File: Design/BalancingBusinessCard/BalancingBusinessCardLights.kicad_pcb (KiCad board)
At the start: 2 copper layers, 51 x 89 mm, 38 parts, among them J101 Conn_02x01, SW101 SW_Push, U101 ATtiny261A-MU, U401 LIS3DHTR, U402 MCP1640DCH

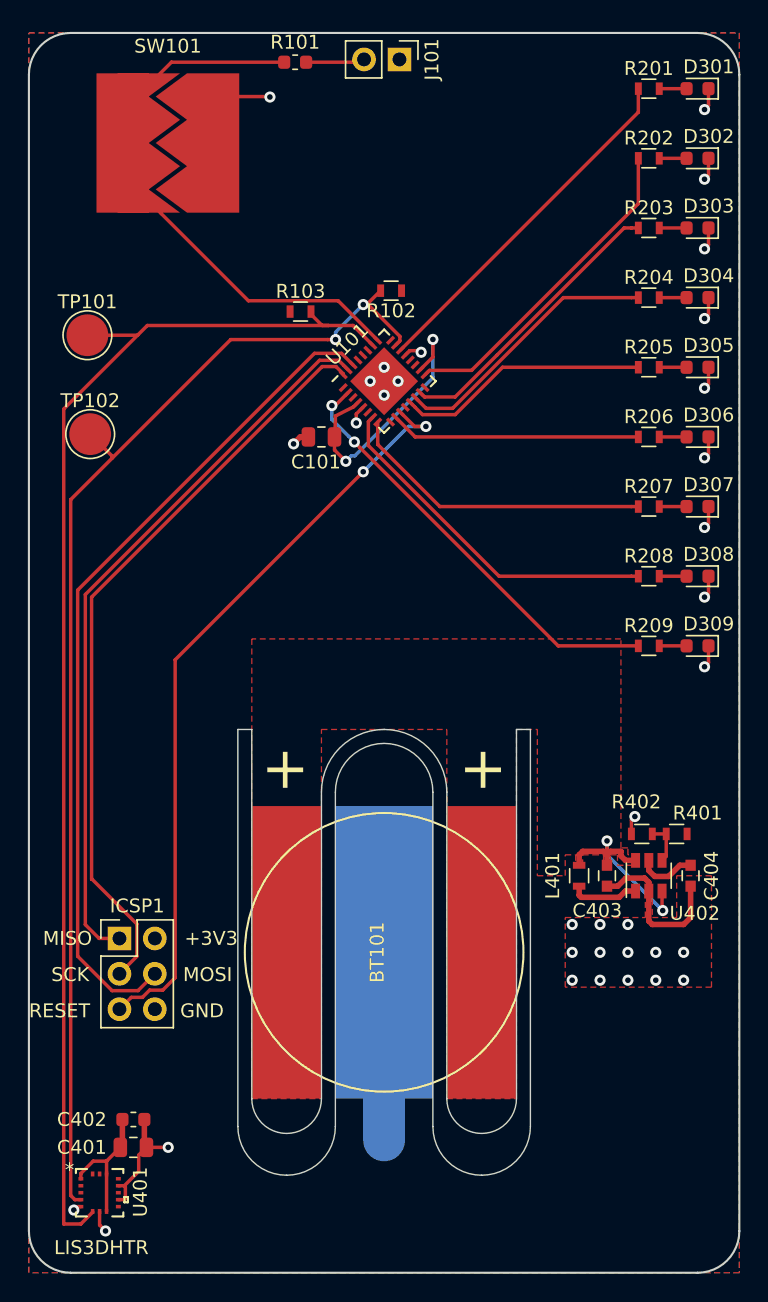
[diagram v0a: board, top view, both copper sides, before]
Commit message: Added explicit routing for most ground and power wires
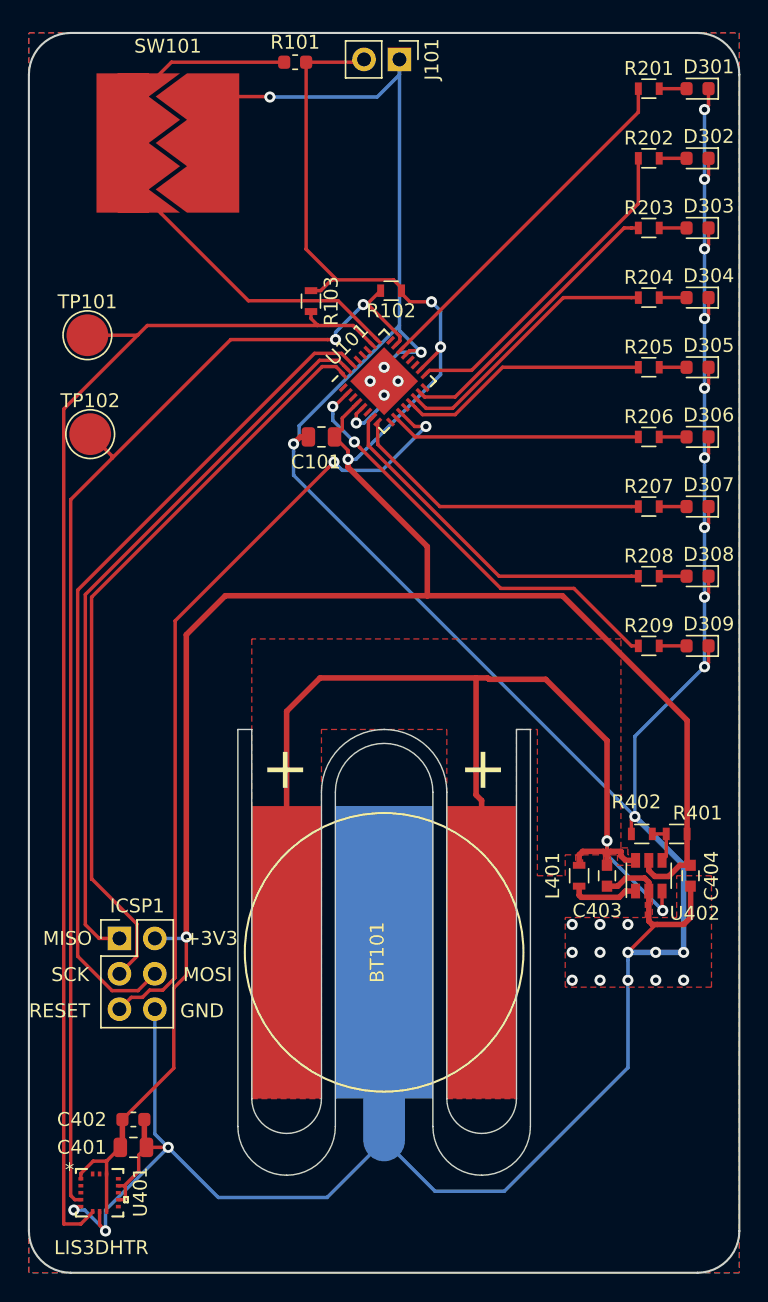
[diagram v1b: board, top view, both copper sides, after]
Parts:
- moved R103 1.06 mm to (200.2, 69.2), turned to 270 degrees
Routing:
- net GND: track 76.0 -> 305.3 mm
- net +3V3: track 37.7 -> 169.1 mm, vias 2 -> 4
- net +BATT: track 16.1 -> 86.4 mm
- net /RESET: track 55.0 -> 57.1 mm
- net /SDA: track 91.6 -> 91.0 mm

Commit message: Moved all components to top half of board
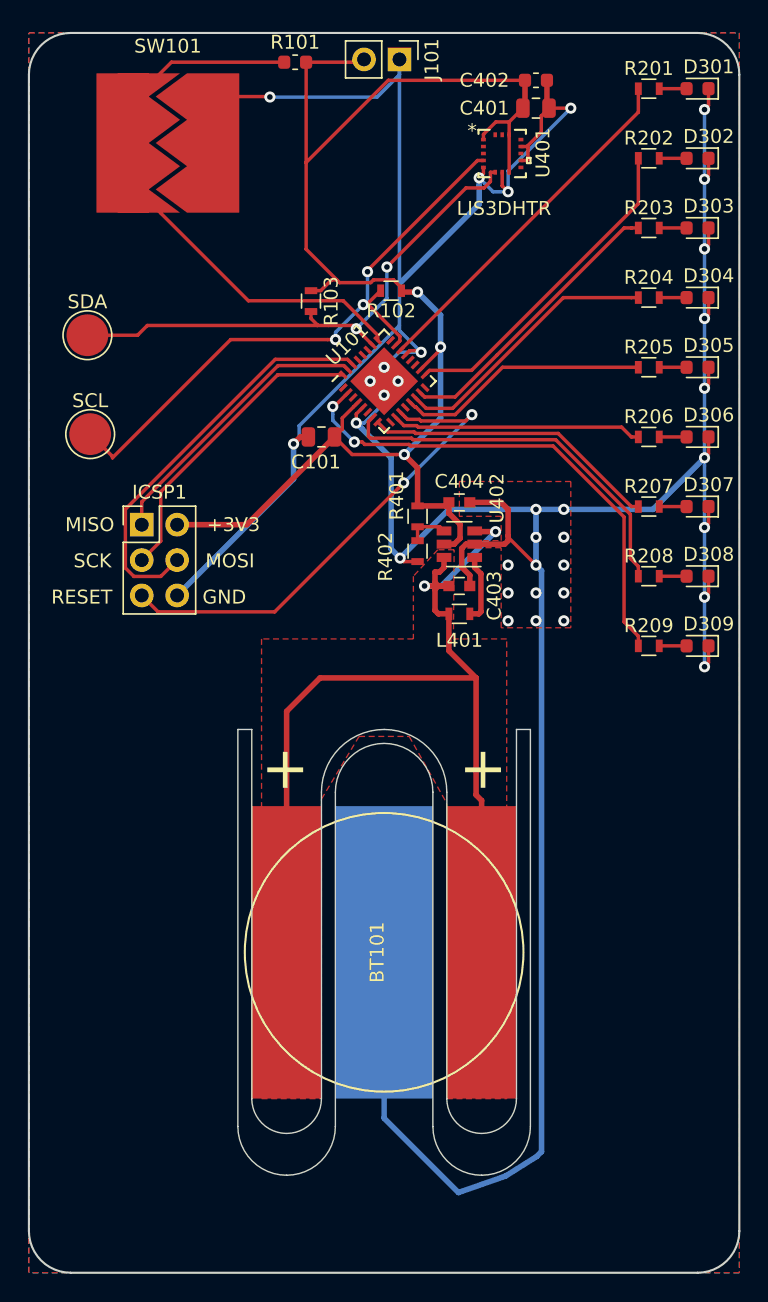
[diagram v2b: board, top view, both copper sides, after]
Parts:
- moved C401 80.0 mm to (216.4, 55.4)
- moved C402 80.0 mm to (216.4, 53.4)
- moved U401 80.0 mm to (214.0, 58.7)
- moved C404 31.5 mm to (210.9, 83.7), turned to 0 degrees
- moved ICSP1 29.7 mm to (188.1, 85.3)
- moved R401 29.4 mm to (207.9, 84.7), turned to 270 degrees
- moved U402 27.4 mm to (210.9, 86.7), turned to 180 degrees
- moved R402 25.9 mm to (207.9, 87.2), turned to 270 degrees
- moved C403 23.3 mm to (210.9, 89.7), turned to 0 degrees
- moved L401 20.7 mm to (210.9, 91.7), turned to 180 degrees
- renumbered TP102 to SCL, TP101 to SDA
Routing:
- net +3V3: track 169.1 -> 106.2 mm, vias 4 -> 3
- net /SDA: track 91.0 -> 38.9 mm, vias 0 -> 2
- net /SCL: track 86.3 -> 45.4 mm, vias 2 -> 3
- net /SCK: track 54.1 -> 22.0 mm
- net /MISO: track 52.7 -> 20.6 mm
- net /MOSI: track 60.5 -> 29.6 mm
- net /RESET: track 57.1 -> 35.6 mm
- net +BATT: track 86.4 -> 73.5 mm
- net GND: track 305.3 -> 299.2 mm
- net /LED_8: track 31.2 -> 36.0 mm
- net /LED_7: track 25.4 -> 27.3 mm
- net /LED_6: track 22.2 -> 21.2 mm
